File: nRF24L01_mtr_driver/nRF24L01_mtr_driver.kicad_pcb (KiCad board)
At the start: 4 copper layers, 59.8 x 39.9 mm, 137 parts, among them J1 Micro USB, J2 I/O, J4 VBAT, J5 MTR, J6 SERVO, J7 ICSP, Q1 AO4484, Q2 AO4484, Q3 AO4484, Q4 AO4484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

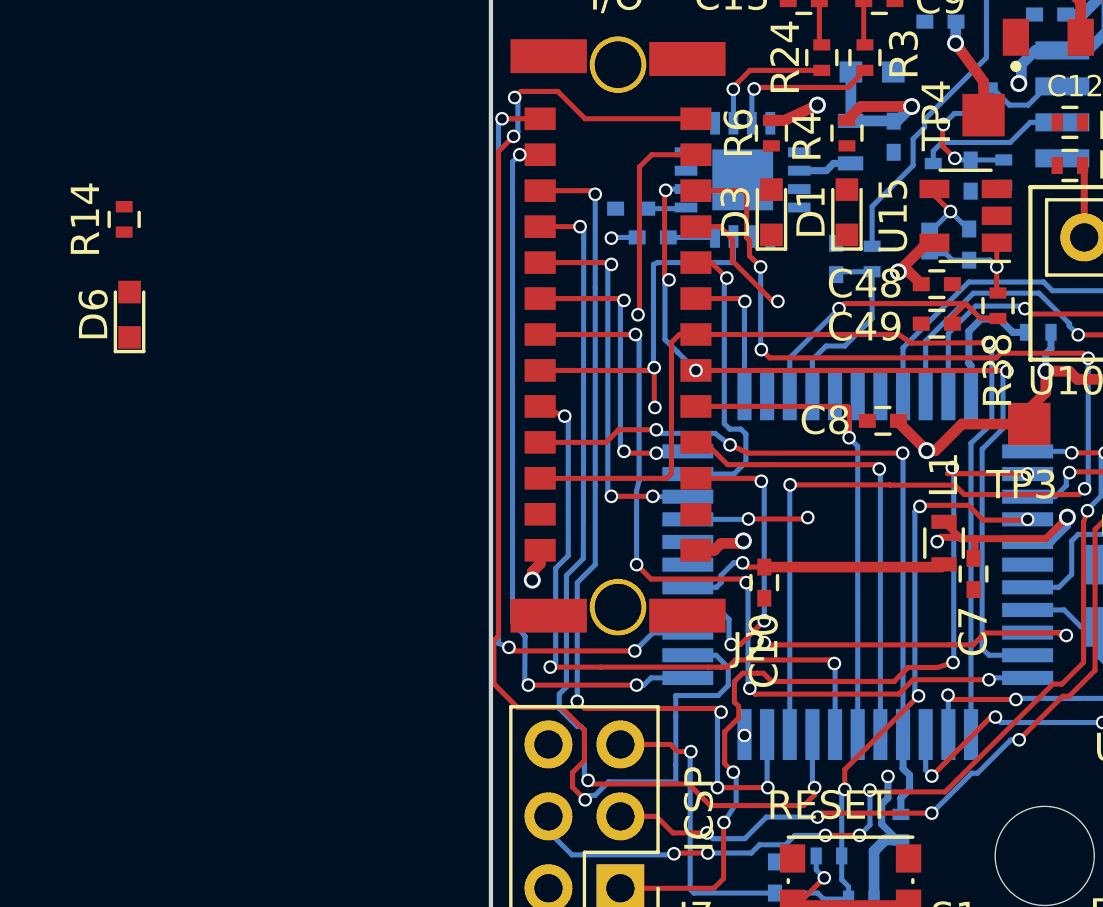
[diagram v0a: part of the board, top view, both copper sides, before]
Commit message: added LED1
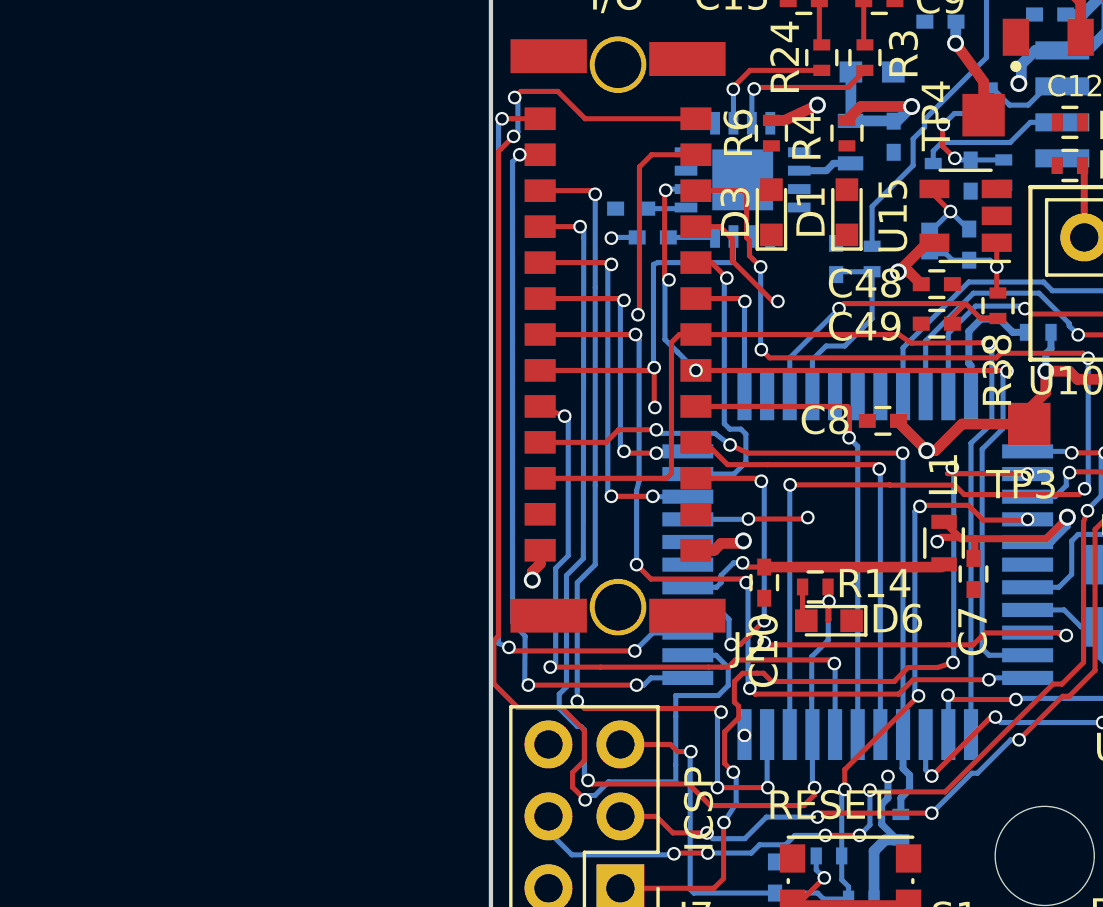
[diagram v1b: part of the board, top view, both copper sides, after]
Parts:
- moved R14 27.6 mm to (72.7, 72.2), turned to 180 degrees
- moved D6 27.0 mm to (73.2, 73.4), turned to 180 degrees
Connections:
- J2 pad 20: /PC0 -> /LED1
- U1 pad 19: /PC0 -> /LED1
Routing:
- net /LED1: track 0.00 -> 39.4 mm, vias 0 -> 4
- net /PC0: track 32.6 -> 0.00 mm, vias 3 -> 0
- net Net-(D6-Pad2): track 0.00 -> 1.25 mm

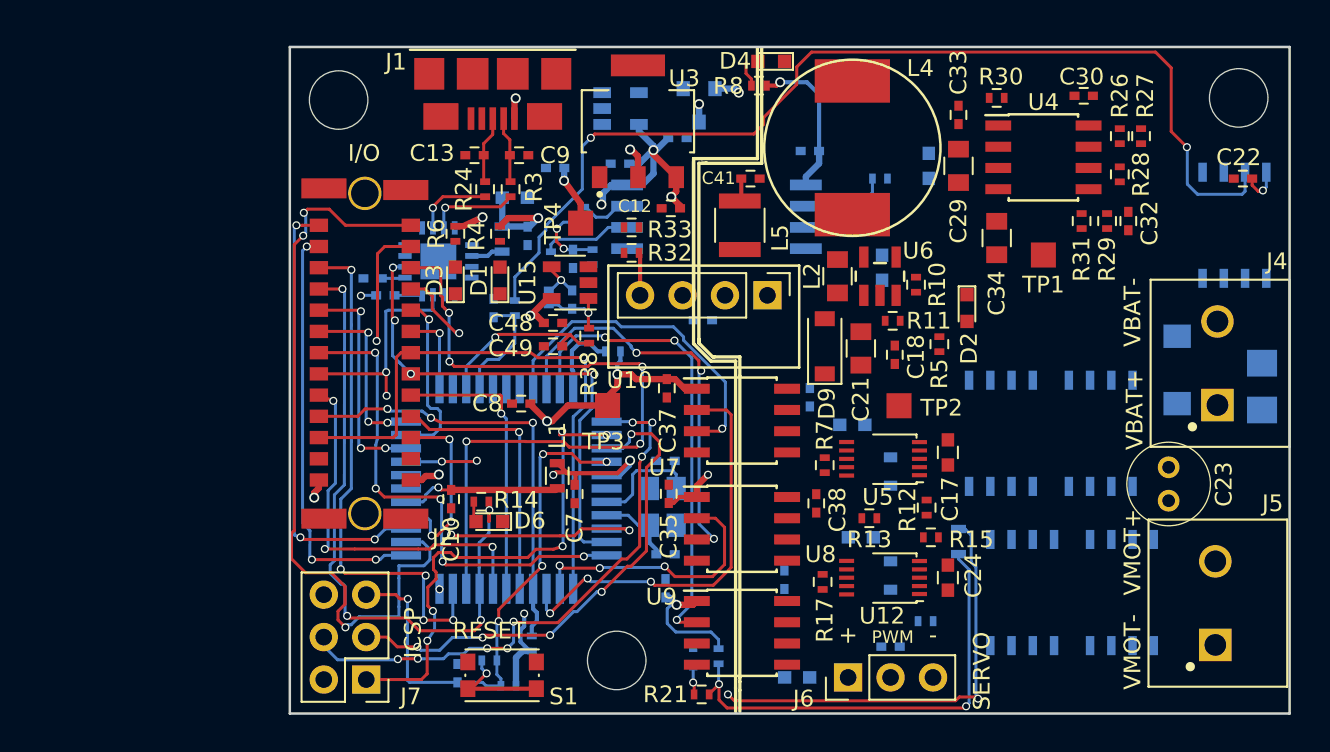
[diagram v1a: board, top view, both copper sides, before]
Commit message: 4-layer, most of the routing done (logic + pwr)
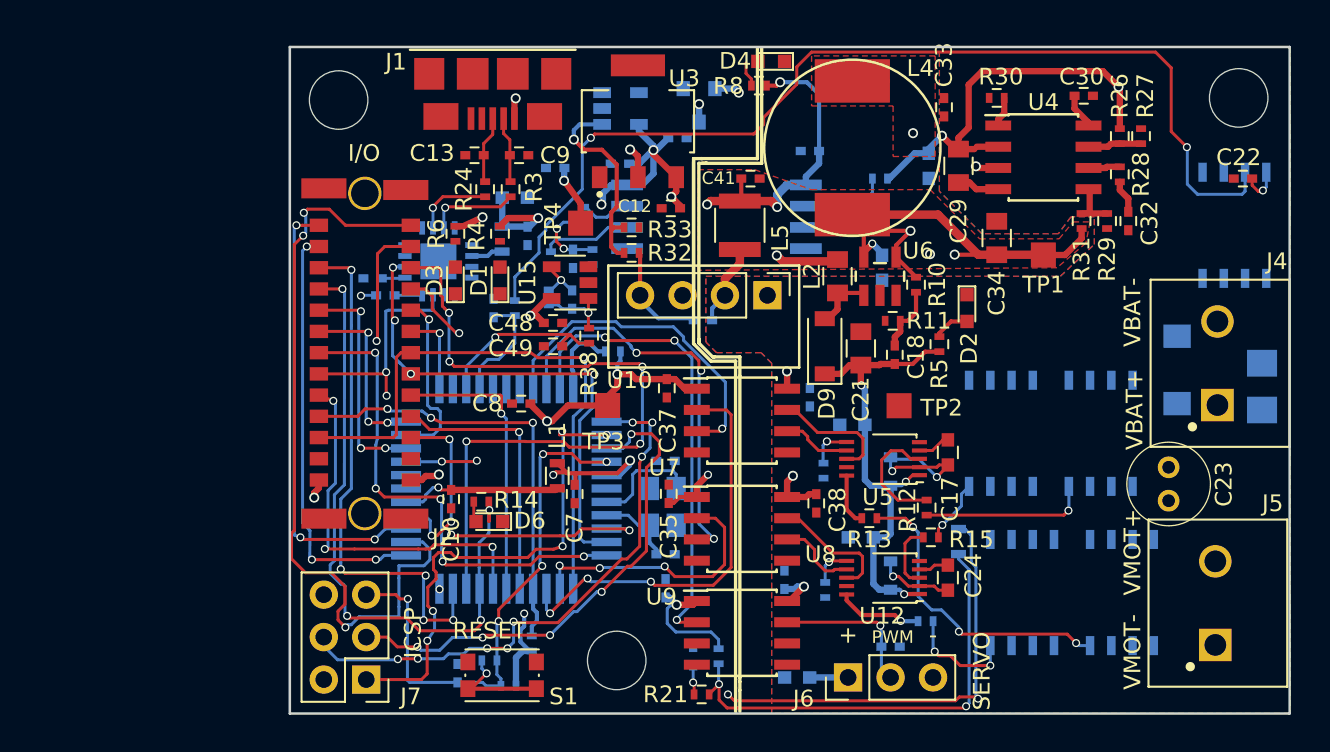
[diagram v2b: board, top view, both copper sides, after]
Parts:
- R17, R7: moved to B.Cu
- moved C33 0.98 mm to (100.4, 48.6)
- moved R17 0.51 mm to (93.2, 77.4)
- moved R7 0.34 mm to (93.1, 70.3)
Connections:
- net Net-(C33-Pad1) renamed /SW
- C14 pad 1: VBAT -> /VBAT_S
- C29 pad 1: VBAT -> /VBAT_S
- R19 pad 1: VBAT -> /VBAT_S
- R26 pad 2: VBAT -> /VBAT_S
- U4 pad 2: VBAT -> /VBAT_S
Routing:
- net 5V0_PWR: track 10.7 -> 97.1 mm, vias 1 -> 11
- net 12V_PWR: track 0.00 -> 27.8 mm, vias 0 -> 3
- net /VBAT_S: track 0.00 -> 24.4 mm, vias 0 -> 2
- net Net-(Q1-Pad4): track 0.00 -> 18.4 mm, vias 0 -> 3
- net Net-(R32-Pad2): track 0.00 -> 12.4 mm, vias 0 -> 1
- net Net-(Q2-Pad4): track 0.00 -> 10.1 mm, vias 0 -> 1
- net /SERVO_PWM: track 0.00 -> 9.02 mm, vias 0 -> 1
- net Net-(C17-Pad1): track 0.00 -> 8.60 mm, vias 0 -> 2
- net /SW: track 0.00 -> 8.29 mm, vias 0 -> 2
- net /IN2: track 0.00 -> 7.52 mm
- net /IN1: track 0.00 -> 7.31 mm
- net Net-(R12-Pad2): track 0.00 -> 7.21 mm
- net Net-(Q4-Pad4): track 0.00 -> 6.72 mm, vias 0 -> 2
- net Net-(R16-Pad1): track 0.00 -> 5.15 mm, vias 0 -> 1
- net Net-(C42-Pad2): track 0.00 -> 4.91 mm
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- added copper zone on In1.Cu, net /H1_out
- added copper zone on In2.Cu, net /H1_out
- added copper zone on In1.Cu, net /H2_out
- added copper zone on In2.Cu, net /H2_out
- added copper zone on F.Cu, net /SW
- added copper zone on In1.Cu, net /SW
- added copper zone on In1.Cu, net /VBAT_S
- added copper zone on In2.Cu, net /VBAT_S
- added copper zone on F.Cu, net 5V0_PWR
- added copper zone on In1.Cu, net 5V0_PWR
- added copper zone on B.Cu, net GND_PWR
- added copper zone on F.Cu, net GND_PWR
- added copper zone on In1.Cu, net GND_PWR
- added copper zone on In2.Cu, net GND_PWR
- added copper zone on In1.Cu, net Net-(C23-Pad1)
- added copper zone on In2.Cu, net Net-(C23-Pad1)

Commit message: copper pour plane zones done
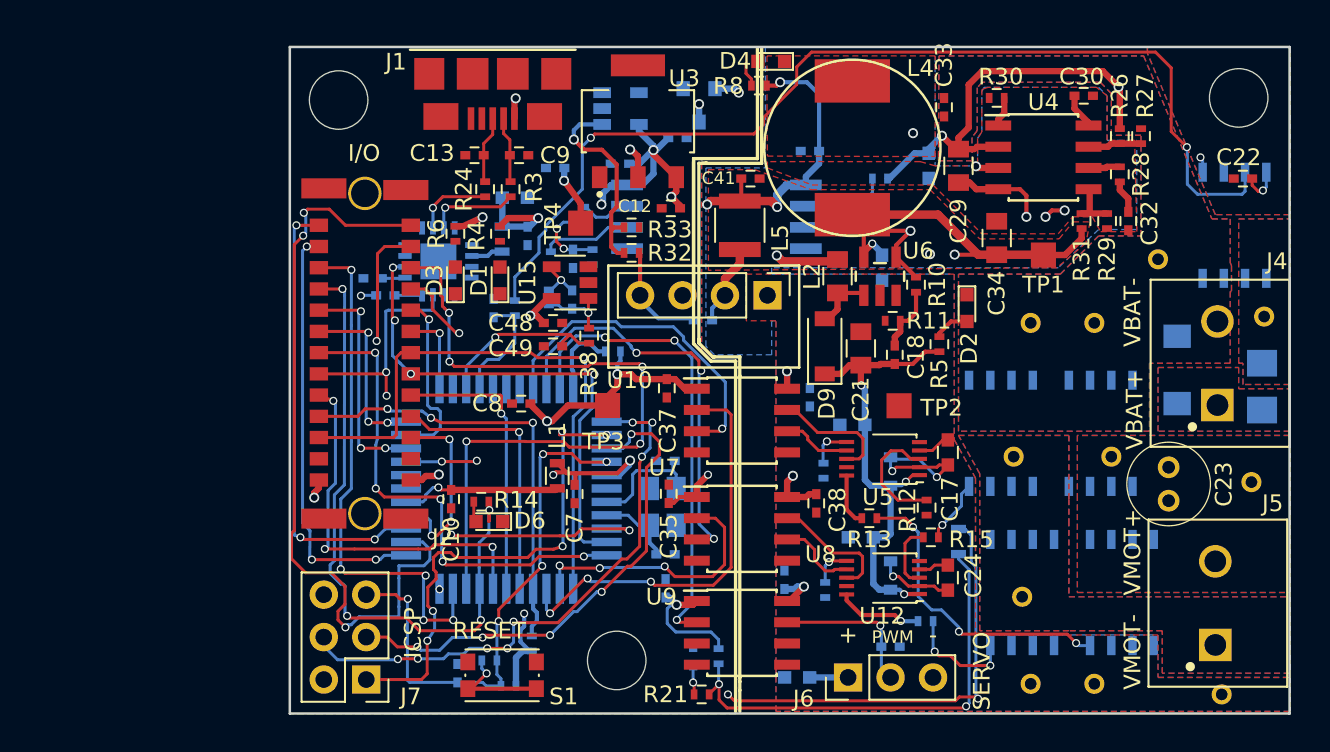
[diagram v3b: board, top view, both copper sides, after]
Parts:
- added REF**: THERMO VIA, mc-footprints:SINGLE_THERMO_VIA, F.Cu at (118.7, 71.0)
- added REF**: THERMO VIA, mc-footprints:SINGLE_THERMO_VIA, F.Cu at (105.5, 61.5)
- added REF**: THERMO VIA, mc-footprints:SINGLE_THERMO_VIA, F.Cu at (113.2, 57.7)
- added REF**: THERMO VIA, mc-footprints:SINGLE_THERMO_VIA, F.Cu at (110.4, 69.5)
- added REF**: THERMO VIA, mc-footprints:SINGLE_THERMO_VIA, F.Cu at (104.5, 69.5)
- added REF**: THERMO VIA, mc-footprints:SINGLE_THERMO_VIA, F.Cu at (105.0, 77.9)
- added REF**: THERMO VIA, mc-footprints:SINGLE_THERMO_VIA, F.Cu at (109.3, 83.1)
- added REF**: THERMO VIA, mc-footprints:SINGLE_THERMO_VIA, F.Cu at (105.5, 83.1)
- added REF**: THERMO VIA, mc-footprints:SINGLE_THERMO_VIA, F.Cu at (117.0, 83.7)
- added REF**: THERMO VIA, mc-footprints:SINGLE_THERMO_VIA, F.Cu at (109.3, 61.5)
- added REF**: THERMO VIA, mc-footprints:SINGLE_THERMO_VIA, F.Cu at (119.5, 61.1)
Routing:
- net Net-(Q2-Pad4): track 10.1 -> 0.00 mm, vias 1 -> 0
- net GND_PWR: track 6.42 -> 12.0 mm, vias 0 -> 3
- net GNDA: track 26.1 -> 27.1 mm, vias 2 -> 3
- added copper zone on B.Cu, net (none)
- added copper zone on F.Cu, net (none)
- added copper zone on B.Cu, net /H1_out
- added copper zone on F.Cu, net /H1_out
- added copper zone on B.Cu, net /H2_out
- added copper zone on F.Cu, net /H2_out
- added copper zone on B.Cu, net /VBAT_S
- added copper zone on F.Cu, net /VBAT_S
- added copper zone on B.Cu, net GNDA
- added copper zone on F.Cu, net GNDA
- added copper zone on B.Cu, net VBAT
- added copper zone on F.Cu, net VBAT
- added copper zone on In1.Cu, net VBAT
- added copper zone on In2.Cu, net VBAT

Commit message: All pour planes finalized
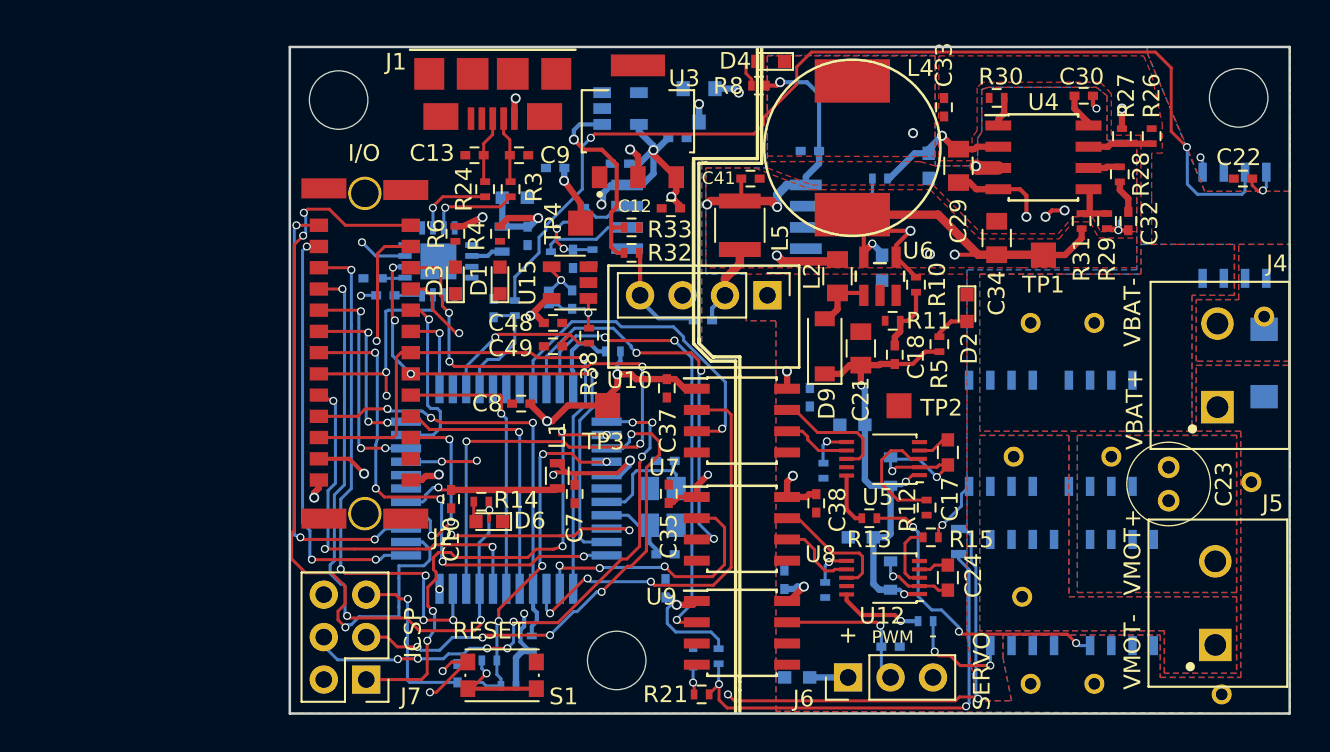
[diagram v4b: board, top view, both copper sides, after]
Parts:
- removed F1: F3542CT-ND, Resistors:1206
- removed the REF** at (113.2, 57.7)
- moved D8 6.85 mm to (119.5, 61.8), turned to 270 degrees
- moved R26 1.91 mm to (112.8, 50.3)
- moved R27 1.14 mm to (111.0, 50.3)
- moved J4 0.13 mm to (116.7, 64.0)
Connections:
- C23 pad 1: Net-(C23-Pad1) -> VBAT
- D8 pad 1: Net-(C23-Pad1) -> VBAT
- J4 pad 1: Net-(C23-Pad1) -> GND_PWR
- J4 pad 2: GND_PWR -> VBAT
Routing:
- net /VBAT_S: track 24.4 -> 8.04 mm, vias 2 -> 1
- net GNDA: track 27.1 -> 37.8 mm, vias 3 -> 7
- net GND_PWR: track 12.0 -> 15.9 mm, vias 3 -> 6
- net Net-(R26-Pad1): track 3.22 -> 3.73 mm
- added copper zone on In1.Cu, net 12V_PWR
- removed copper zone on B.Cu, net (none)
- removed copper zone on F.Cu, net (none)
- removed copper zone on In1.Cu, net Net-(C23-Pad1)
- removed copper zone on In2.Cu, net Net-(C23-Pad1)

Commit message: fixed VABT and GND_PWR planes for C23, 43 unconnections left
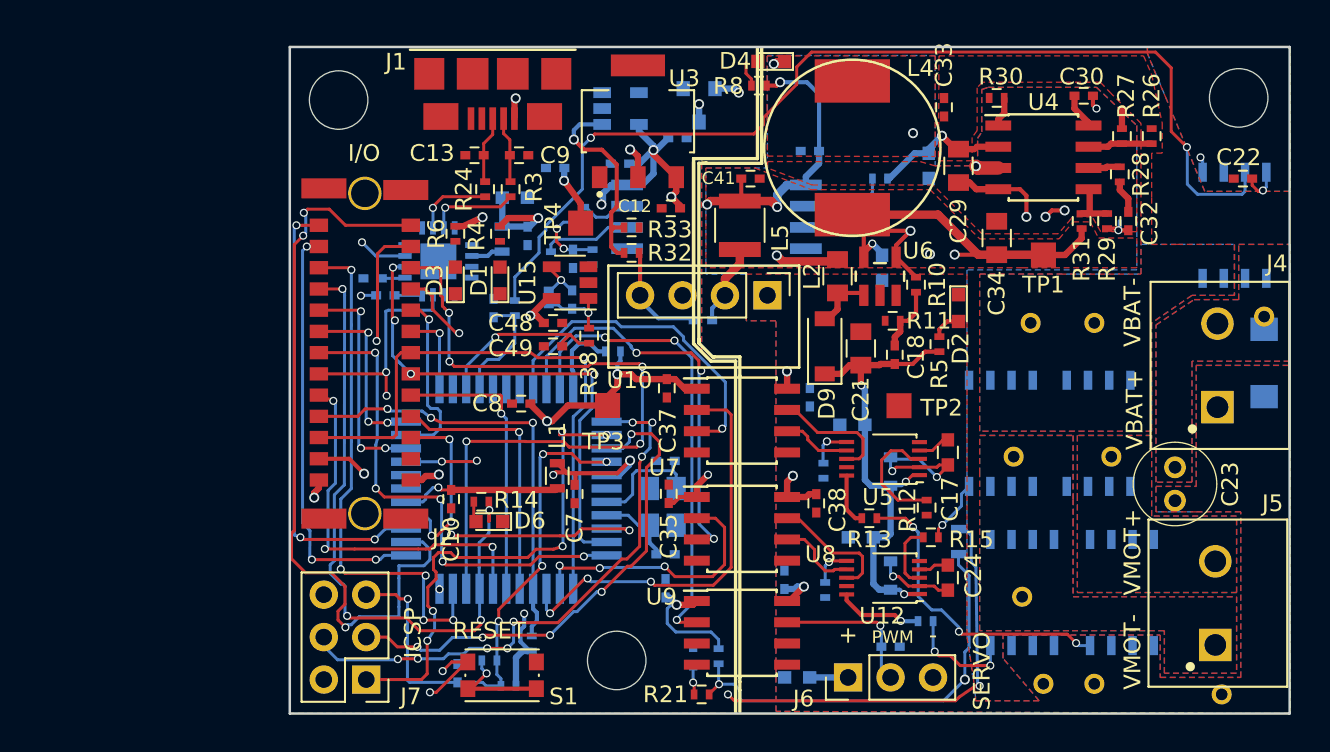
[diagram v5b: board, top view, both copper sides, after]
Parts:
- removed the REF** at (118.7, 71.0)
- moved REF** 0.76 mm to (106.3, 83.1)
- moved D2 0.51 mm to (101.2, 60.6)
- moved C23 0.38 mm to (114.2, 70.1)
- moved Q2 0.13 mm to (109.6, 68.1)
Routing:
- net Net-(R21-Pad1): track 27.5 -> 25.9 mm
- net GND_PWR: track 15.9 -> 16.6 mm

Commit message: 7 unconnections let
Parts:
- added REF**: THERMO VIA, mc-footprints:SINGLE_THERMO_VIA, F.Cu at (119.6, 78.6)
- added REF**: THERMO VIA, mc-footprints:SINGLE_THERMO_VIA, F.Cu at (119.6, 83.2)
- R16: moved to F.Cu
- moved REF** 13.4 mm to (119.4, 70.5)
- moved REF** 2.77 mm to (112.0, 83.8)
- moved REF** 1.91 mm to (108.2, 82.9)
- moved C33 0.22 mm to (100.5, 48.4)
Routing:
- net GNDA: track 37.4 -> 128.1 mm, vias 7 -> 31
- net /ADC2: track 1.76 -> 77.5 mm, vias 1 -> 3
- net 5V0_MCU: track 177.5 -> 135.7 mm, vias 15 -> 16
- net /VBAT_S: track 8.04 -> 26.3 mm, vias 1 -> 10
- net 3V3_MCU: track 39.4 -> 23.5 mm, vias 4 -> 3
- net Net-(C6-Pad1): track 1.40 -> 16.6 mm
- net /LED1: track 39.4 -> 53.4 mm, vias 4 -> 6
- net 12V_PWR: track 27.8 -> 41.7 mm, vias 3 -> 10
- net /H1_out: track 1.96 -> 12.5 mm
- net GND_PWR: track 16.6 -> 26.1 mm, vias 6 -> 12
- net Net-(Q2-Pad4): track 0.00 -> 9.09 mm, vias 0 -> 1
- net /H2_out: track 1.81 -> 6.08 mm, vias 0 -> 1
- net Net-(C47-Pad1): track 2.93 -> 6.53 mm
- net Net-(Q5-Pad1): track 0.00 -> 2.75 mm
- net /SW: track 8.29 -> 10.9 mm
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
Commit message: finsihed routing, added 3D model for IO connector, still needs silckcreen touchup
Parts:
- moved R26 0.22 mm to (112.6, 50.4)
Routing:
- net 5V0_MCU: track 135.7 -> 173.7 mm
- net GNDA: track 128.1 -> 139.8 mm, vias 31 -> 37
- net /VBAT_S: track 26.3 -> 31.3 mm, vias 10 -> 13
- net 3V3_MCU: track 23.5 -> 24.9 mm, vias 3 -> 4
- net /RX0: track 36.5 -> 35.3 mm
- net /PC3: track 25.8 -> 25.2 mm
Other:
- board size 59.8 x 39.9 mm -> 60.1 x 39.9 mm
